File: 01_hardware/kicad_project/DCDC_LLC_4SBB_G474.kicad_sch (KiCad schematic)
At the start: 0 parts

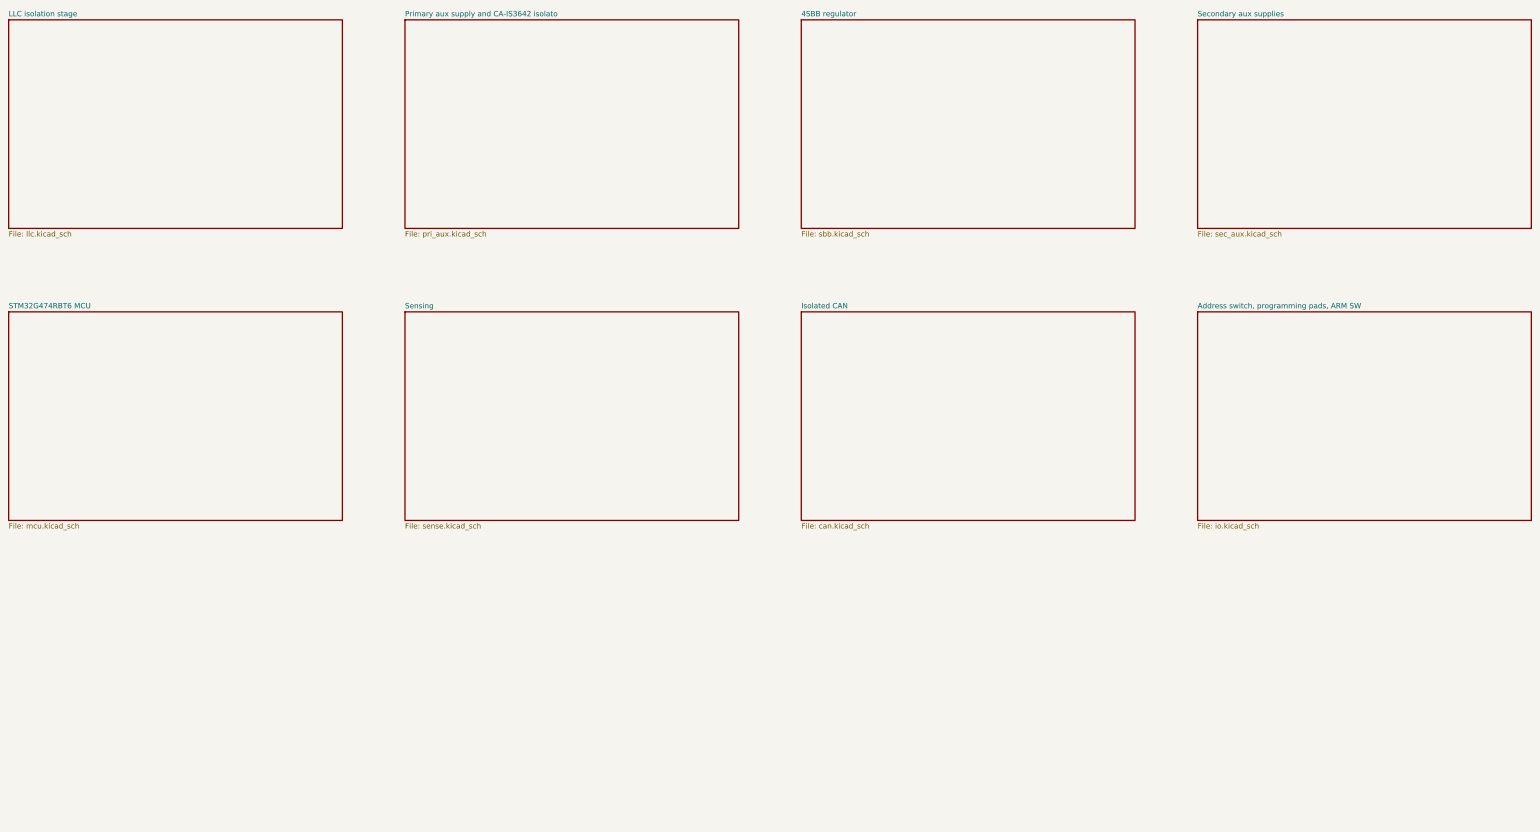
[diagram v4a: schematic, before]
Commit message: Rev E: isolated flyback aux supply, VREF+ back to 3.3 V, 1 oz re-layout
- New isolated aux flyback (sheet iso_pwr): UC3843B U20 from +10V_P, FDN86246 Q11,
  PA3855.006NLT EP13 T2, SS110 D9 -> isolated +10 V; secondary regulation TL431 U22 +
  EL357N opto U21 into COMP; RCD clamp D8/R116/C94; 2 A primary limit (R114)
- Secondary rails from the flyback, not VBUS: +10 V -> U4 10->5 V -> U5 TLV75533 3.3 V;
  MCU, CAN and drivers up before the LLC starts
- U12 -> CA-IS3742LW (data only); REF3030 U19 removed, VREF+ = +3V3A (3.3 V full scale)
- PCB re-placed / re-routed for 1 oz outer / 0.5 oz inner: power pours on F.Cu, In1 solid
  ground planes, gate loops as tight HO/HS pairs, 1.7 mm power-via pitch, per-pad GND vias
  in the MCU area; copper loss ~0.5 W at 50 W (03_calculations/copper_check.txt)
- DRC (JLC rules) 0 errors / 0 unconnected; netlist 148 nets / 284 parts 0 errors;
  isolation bands clear; BOM / JLC BOM+CPL / Gerbers / PDFs / design notes / READMEs updated
- Scripts: 04_scripts/pcb5 (placement, pours, routing, floods, island vias, silk),
  03_calculations/flyback_aux.py, copper_check.py

Co-Authored-By: Claude Opus 5.5 <noreply@anthropic.com>
Claude-Session: https://claude.ai/code/session_01A35wrnwFKLPSaRSxxHs471
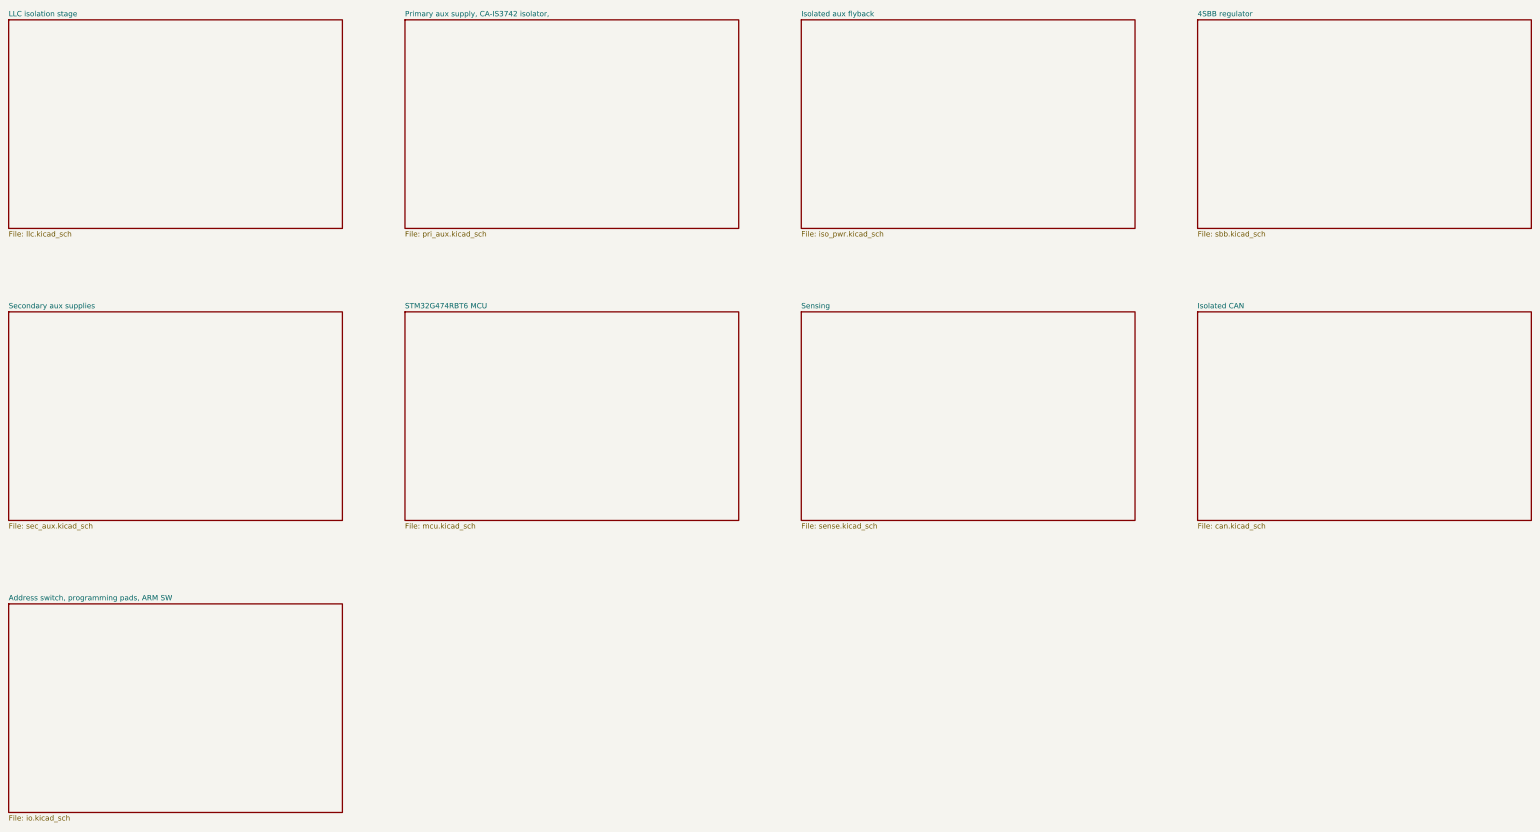
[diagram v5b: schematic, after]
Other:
- removed sheet Primary aux supply and CA-IS3642 isolato
- added sheet Isolated aux flyback (iso_pwr.kicad_sch)
- added sheet Primary aux supply, CA-IS3742 isolator,  (pri_aux.kicad_sch)

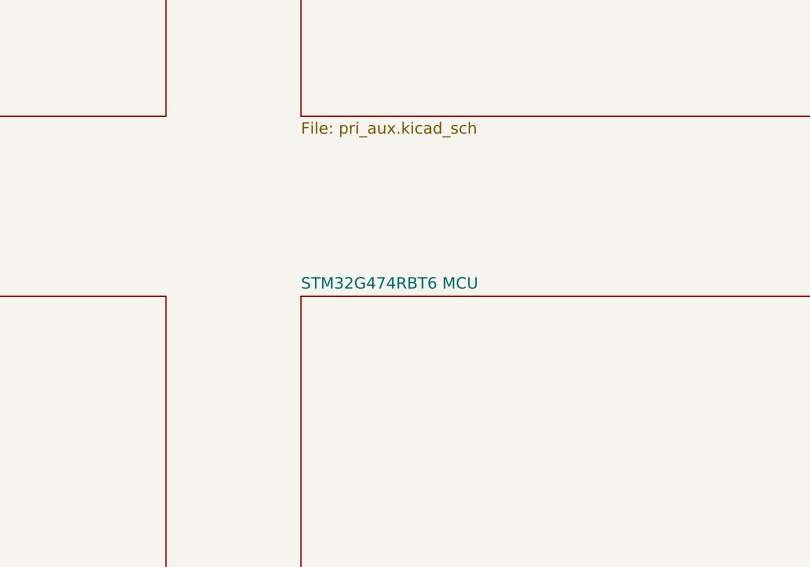
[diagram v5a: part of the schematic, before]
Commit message: Rev E BOM: in-stock LCSC first source for every part; 2nd/3rd sources checked
- First sources swapped (same footprints, layout unchanged): U1 STM32G474RBT3,
  Q2/Q3/Q5/Q6 NCEP068N10G, 10k 0402 FOJAN, 100n 0402 merged onto C307331,
  1u 0402 CCTC, R62/R63/R89/R82, FB1 Murata BLM18KG601SN1D, L2/L3 cjiang
  FNR5040S470MT, C82 KEMET C0G (was X7R), RS1 Milliohm HoJLR2512, SS110 MDD
- LCSC part numbers for the hand-soldered headers (J1-J5, J7, JP1)
- Schematic and PCB fields, BOM, JLC BOM/CPL, PDFs and design notes regenerated;
  netlist check 0 errors, DRC unchanged
- BOM_sourcing_revE.xlsx: live LCSC stock 2026-10-20, 2nd/3rd sources checked
  for pinout / land pattern / ratings, PCB reserve options for T2 and U9

Co-Authored-By: Claude Opus 5.5 <noreply@anthropic.com>
Claude-Session: https://claude.ai/code/session_01A35wrnwFKLPSaRSxxHs471
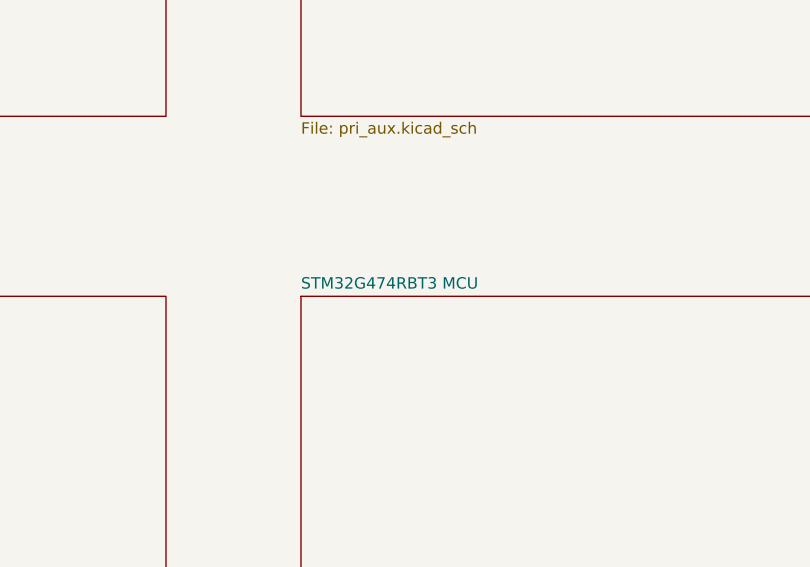
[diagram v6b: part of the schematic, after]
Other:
- sheet STM32G474RBT6 MCU renamed STM32G474RBT3 MCU
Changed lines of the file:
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@@
     (date "2026-10-19")
     (rev "E")
-    (comment 1 "Isolated 12-48 V -> 1.5-48 V / 5 A / 50 W; STM32G474RBT6; isolated CAN")
+    (comment 1 "Isolated 12-48 V -> 1.5-48 V / 5 A / 50 W; STM32G474RBT3; isolated CAN")
     (comment 2 "Sheets connect through global labels and power symbols")
   )
@@
     (stroke (width 0.1524) (type solid))
     (fill (color 0 0 0 0))
-    (property "Sheet name" "STM32G474RBT6 MCU" (id 0) (at 120 109.3 0)
+    (property "Sheet name" "STM32G474RBT3 MCU" (id 0) (at 120 109.3 0)
       (effects (font (size 1.27 1.27)) (justify left bottom))
     )
@@
     )
     (path "/cae3053b-20cc-4557-ac72-ae2b74fe45c3/b8495fbe-d60e-461a-9db5-3653245d483e"
-      (reference "Q5") (unit 1) (value "NCEP0160AG") (footprint "Package_TO_SOT_SMD:TDSON-8-1")
+      (reference "Q5") (unit 1) (value "NCEP068N10G") (footprint "Package_TO_SOT_SMD:TDSON-8-1")
     )
     (path "/cae3053b-20cc-4557-ac72-ae2b74fe45c3/7d59ffc5-fd0e-4fcb-a4c0-caf0214c72cb"
-      (reference "Q6") (unit 1) (value "NCEP0160AG") (footprint "Package_TO_SOT_SMD:TDSON-8-1")
+      (reference "Q6") (unit 1) (value "NCEP068N10G") (footprint "Package_TO_SOT_SMD:TDSON-8-1")
     )
     (path "/cae3053b-20cc-4557-ac72-ae2b74fe45c3/65d74259-5126-4e8a-804f-47846c3f4761"
@@
     )
     (path "/6a8270f3-b6c3-406d-a936-9cd18ffa1121/9a74c2d6-7770-4647-8700-4a27a1e9df52"
-      (reference "C82") (unit 1) (value "47n C0G 50V") (footprint "Capacitor_SMD:C_0805_2012Metric")
+      (reference "C82") (unit 1) (value "47n C0G 25V") (footprint "Capacitor_SMD:C_0805_2012Metric")
     )
     (path "/6a8270f3-b6c3-406d-a936-9cd18ffa1121/3290ab0b-8622-4cb6-ba37-08be6992472a"
@@
     )
     (path "/6b39169d-dfa3-4565-a594-5f779a6e82b8/b9af9a14-dd26-4d4a-8ead-b6f1580abbe5"
-      (reference "Q2") (unit 1) (value "NCEP0160AG") (footprint "Package_TO_SOT_SMD:TDSON-8-1")
+      (reference "Q2") (unit 1) (value "NCEP068N10G") (footprint "Package_TO_SOT_SMD:TDSON-8-1")
     )
     (path "/6b39169d-dfa3-4565-a594-5f779a6e82b8/ba1fc9a8-c44f-4774-8272-5e58e868ca04"
-      (reference "Q3") (unit 1) (value "NCEP0160AG") (footprint "Package_TO_SOT_SMD:TDSON-8-1")
+      (reference "Q3") (unit 1) (value "NCEP068N10G") (footprint "Package_TO_SOT_SMD:TDSON-8-1")
     )
     (path "/6b39169d-dfa3-4565-a594-5f779a6e82b8/100d591b-4573-4b1c-b449-f9ab9100e952"
@@
     )
     (path "/f23a9dab-1901-42af-8a11-726c269e245c/8dca7355-4cfa-4b04-bb85-4231c36850ce"
-      (reference "U1") (unit 1) (value "STM32G474RBT6") (footprint "Package_QFP:LQFP-64_10x10mm_P0.5mm")
+      (reference "U1") (unit 1) (value "STM32G474RBT3") (footprint "Package_QFP:LQFP-64_10x10mm_P0.5mm")
     )
     (path "/f23a9dab-1901-42af-8a11-726c269e245c/6a6a916d-7bd3-49b7-8e40-8b1d4be032e0"
